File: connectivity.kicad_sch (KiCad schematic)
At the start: 29 parts, among them J3 Conn_02x01, J4 Conn_02x01, J5 Screw_Terminal_01x05, J6 RJ45_Hanrun_HR911105A_Horizon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, U4 TJA1042T-3, U5 LAN8742A, Y2 25 MHz

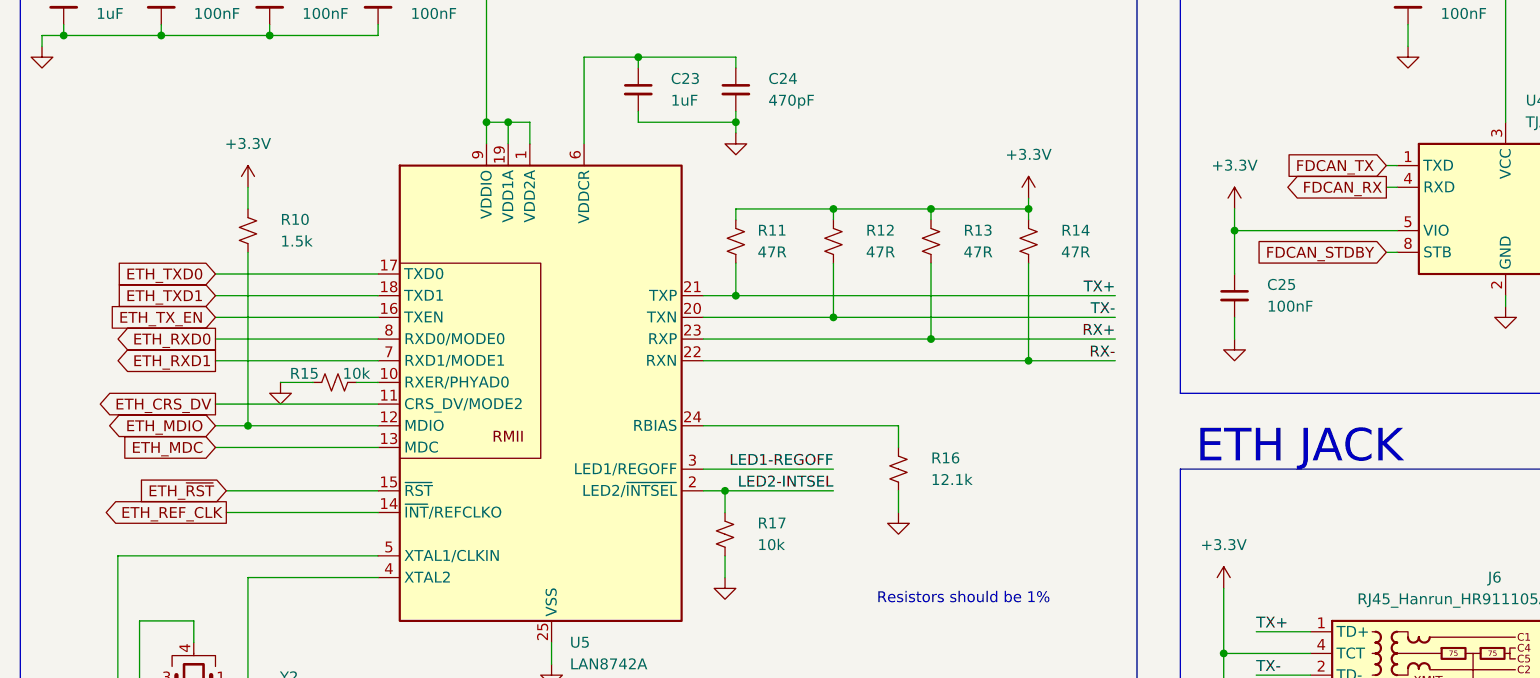
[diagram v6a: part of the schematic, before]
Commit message: Use sheet pins instead of global labels where appropriate
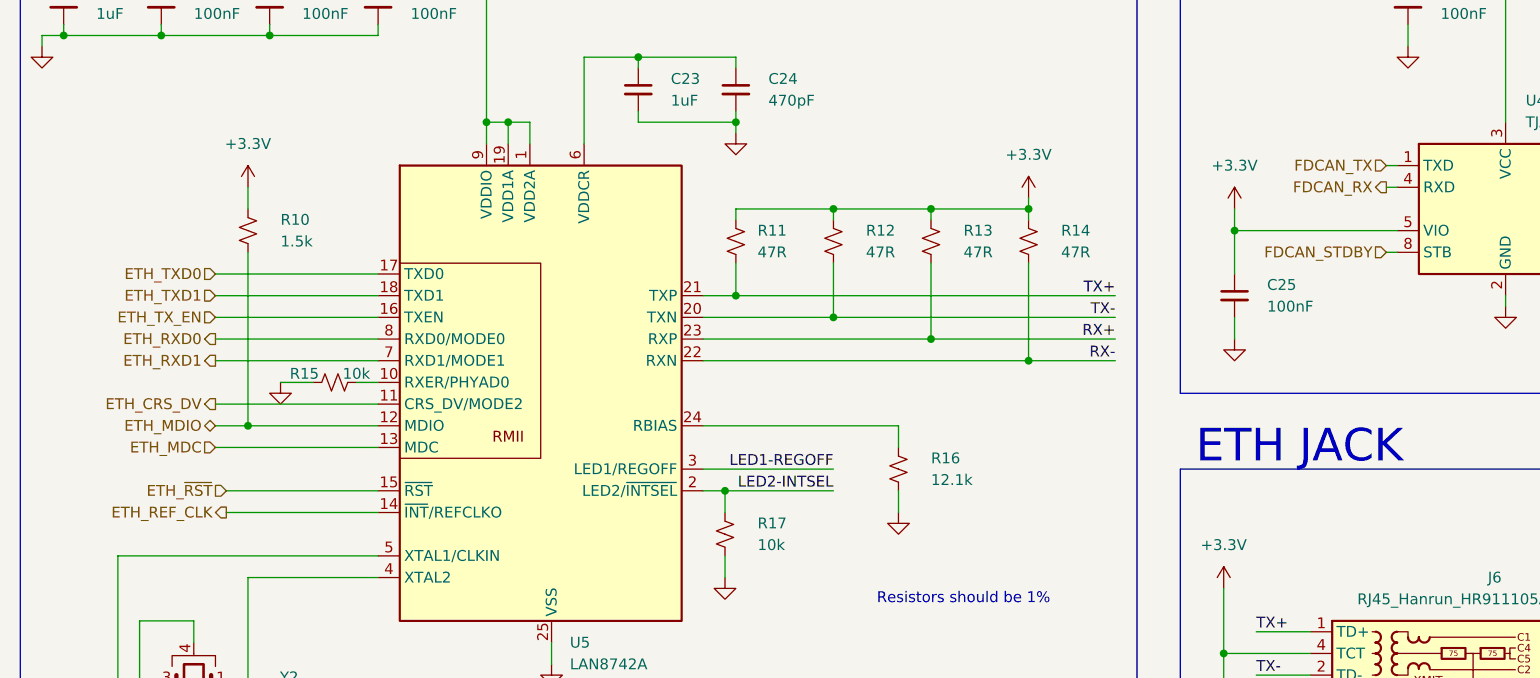
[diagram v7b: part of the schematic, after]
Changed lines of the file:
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@@
 		)
 	)
-	(global_label "FDCAN_STDBY"
-		(shape input)
-		(at 176.53 69.85 180)
-		(fields_autoplaced yes)
+	(hierarchical_label "ETH_RXD1"
+		(shape output)
+		(at 39.37 82.55 180)
 		(effects
 			(font
@@
 			(justify right)
 		)
-		(property "Intersheetrefs" "${INTERSHEET_REFS}"
-			(at 160.8671 69.85 0)
-			(hide yes)
-			(show_name no)
-			(do_not_autoplace no)
-			(effects
-				(font
-					(size 1.27 1.27)
-				)
-				(justify right)
-			)
-		)
 	)
-	(global_label "ETH_TXD1"
+	(hierarchical_label "ETH_~{RST}"
 		(shape input)
-		(at 39.37 74.93 180)
-		(fields_autoplaced yes)
+		(at 40.64 97.79 180)
 		(effects
 			(font
@@
 			(justify right)
 		)
-		(property "Intersheetrefs" "${INTERSHEET_REFS}"
-			(at 27.9964 74.93 0)
-			(hide yes)
-			(show_name no)
-			(do_not_autoplace no)
-			(effects
-				(font
-					(size 1.27 1.27)
-				)
-				(justify right)
-			)
-		)
 	)
-	(global_label "ETH_REF_CLK"
-		(shape output)
-		(at 40.64 100.33 180)
-		(fields_autoplaced yes)
+	(hierarchical_label "FDCAN_STDBY"
+		(shape input)
+		(at 176.53 69.85 180)
 		(effects
 			(font
@@
 			(justify right)
 		)
-		(property "Intersheetrefs" "${INTERSHEET_REFS}"
-			(at 26.0343 100.33 0)
-			(hide yes)
-			(show_name no)
-			(do_not_autoplace no)
-			(effects
-				(font
-					(size 1.27 1.27)
-				)
-				(justify right)
-			)
-		)
 	)
-	(global_label "ETH_CRS_DV"
-		(shape output)
-		(at 39.37 87.63 180)
-		(fields_autoplaced yes)
+	(hierarchical_label "ETH_MDIO"
+		(shape bidirectional)
+		(at 39.37 90.17 180)
 		(effects
 			(font
@@
 			(justify right)
 		)
-		(property "Intersheetrefs" "${INTERSHEET_REFS}"
-			(at 25.4318 87.63 0)
-			(hide yes)
-			(show_name no)
-			(do_not_autoplace no)
-			(effects
-				(font
-					(size 1.27 1.27)
-				)
-				(justify right)
-			)
-		)
 	)
-	(global_label "ETH_MDC"
+	(hierarchical_label "ETH_TXD0"
 		(shape input)
-		(at 39.37 92.71 180)
-		(fields_autoplaced yes)
+		(at 39.37 72.39 180)
 		(effects
 			(font
@@
 			(justify right)
 		)
-		(property "Intersheetrefs" "${INTERSHEET_REFS}"
-			(at 28.015 92.71 0)
-			(hide yes)
-			(show_name no)
-			(do_not_autoplace no)
-			(effects
-				(font
-					(size 1.27 1.27)
-				)
-				(justify right)
-			)
-		)
 	)
-	(global_label "FDCAN_TX"
+	(hierarchical_label "ETH_TXD1"
 		(shape input)
-		(at 176.53 59.69 180)
-		(fields_autoplaced yes)
+		(at 39.37 74.93 180)
 		(effects
 			(font
@@
 			(justify right)
 		)
-		(property "Intersheetrefs" "${INTERSHEET_REFS}"
-			(at 164.5385 59.69 0)
-			(hide yes)
-			(show_name no)
-			(do_not_autoplace no)
-			(effects
-				(font
-					(size 1.27 1.27)
-				)
-				(justify right)
-			)
-		)
 	)
-	(global_label "ETH_TX_EN"
-		(shape input)
-		(at 39.37 77.47 180)
-		(fields_autoplaced yes)
+	(hierarchical_label "FDCAN_RX"
+		(shape output)
+		(at 176.53 62.23 180)
 		(effects
 			(font
@@
 			(justify right)
 		)
-		(property "Intersheetrefs" "${INTERSHEET_REFS}"
-			(at 26.7246 77.47 0)
-			(hide yes)
-			(show_name no)
-			(do_not_autoplace no)
-			(effects
-				(font
-					(size 1.27 1.27)
-				)
-				(justify right)
-			)
-		)
 	)
-	(global_label "FDCAN_RX"
+	(hierarchical_label "ETH_RXD0"
 		(shape output)
-		(at 176.53 62.23 180)
-		(fields_autoplaced yes)
+		(at 39.37 80.01 180)
 		(effects
 			(font
@@
 			(justify right)
 		)
-		(property "Intersheetrefs" "${INTERSHEET_REFS}"
-			(at 164.3822 62.23 0)
-			(hide yes)
-			(show_name no)
-			(do_not_autoplace no)
-			(effects
-				(font
-					(size 1.27 1.27)
-				)
-				(justify right)
-			)
-		)
 	)
-	(global_label "ETH_RXD0"
-		(shape output)
-		(at 39.37 80.01 180)
-		(fields_autoplaced yes)
+	(hierarchical_label "ETH_MDC"
+		(shape input)
+		(at 39.37 92.71 180)
 		(effects
 			(font
@@
 			(justify right)
 		)
-		(property "Intersheetrefs" "${INTERSHEET_REFS}"
-			(at 27.4406 80.01 0)
-			(hide yes)
-			(show_name no)
-			(do_not_autoplace no)
-			(effects
-				(font
-					(size 1.27 1.27)
-				)
-				(justify right)
-			)
-		)
 	)
-	(global_label "ETH_TXD0"
-		(shape input)
-		(at 39.37 72.39 180)
-		(fields_autoplaced yes)
+	(hierarchical_label "ETH_REF_CLK"
+		(shape output)
+		(at 40.64 100.33 180)
 		(effects
 			(font
@@
 			(justify right)
 		)
-		(property "Intersheetrefs" "${INTERSHEET_REFS}"
-			(at 27.5969 72.39 0)
-			(hide yes)
-			(show_name no)
-			(do_not_autoplace no)
-			(effects
-				(font
-					(size 1.27 1.27)
-				)
-				(justify right)
-			)
-		)
 	)
-	(global_label "ETH_MDIO"
-		(shape bidirectional)
-		(at 39.37 90.17 180)
-		(fields_autoplaced yes)
+	(hierarchical_label "ETH_CRS_DV"
+		(shape output)
+		(at 39.37 87.63 180)
 		(effects
 			(font
@@
 			(justify right)
 		)
-		(property "Intersheetrefs" "${INTERSHEET_REFS}"
-			(at 26.3665 90.17 0)
-			(hide yes)
-			(show_name no)
-			(do_not_autoplace no)
-			(effects
-				(font
-					(size 1.27 1.27)
-				)
-				(justify right)
-			)
-		)
 	)
-	(global_label "ETH_RXD1"
-		(shape output)
-		(at 39.37 82.55 180)
-		(fields_autoplaced yes)
+	(hierarchical_label "ETH_TX_EN"
+		(shape input)
+		(at 39.37 77.47 180)
 		(effects
 			(font
@@
 			(justify right)
 		)
-		(property "Intersheetrefs" "${INTERSHEET_REFS}"
-			(at 27.8401 82.55 0)
-			(hide yes)
-			(show_name no)
-			(do_not_autoplace no)
-			(effects
-				(font
-					(size 1.27 1.27)
-				)
-				(justify right)
-			)
-		)
 	)
-	(global_label "ETH_~{RST}"
+	(hierarchical_label "FDCAN_TX"
 		(shape input)
-		(at 40.64 97.79 180)
-		(fields_autoplaced yes)
+		(at 176.53 59.69 180)
 		(effects
 			(font
@@
 			(justify right)
 		)
-		(property "Intersheetrefs" "${INTERSHEET_REFS}"
-			(at 29.793 97.79 0)
-			(hide yes)
-			(show_name no)
-			(do_not_autoplace no)
-			(effects
-				(font
-					(size 1.27 1.27)
-				)
-				(justify right)
-			)
-		)
 	)

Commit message: holy hell 2 adcs
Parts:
- added F5: 500mA, APRLPrints:Fuse_0805_2012Metric, symbol Device:Fuse_Small
- renumbered J3 to J4, J4 to J5, J5 to J6, J6 to J7
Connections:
- net +3.3V: now also J6.2 (Pin_2); no longer J6.1 (Pin_1)
- net +5V: now also F5.1; no longer J6.2 (Pin_2)
- new net: F5.2, J6.1 (Pin_1)
